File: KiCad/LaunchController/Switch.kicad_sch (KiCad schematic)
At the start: 33 parts, among them SW1 SW_Push, SW11 SW_Push, SW12 SW_Push, SW13 SW_Push, SW14 SW_Push, SW15 SW_Push, SW16 SW_Push, SW17 SW_Push, SW18 SW_Push, SW19 SW_Push, SW2 SW_Push, SW20 SW_Push, SW21 SW_Push, SW22 SW_Push, SW23 SW_Push, SW24 SW_Push, SW25 SW_Push

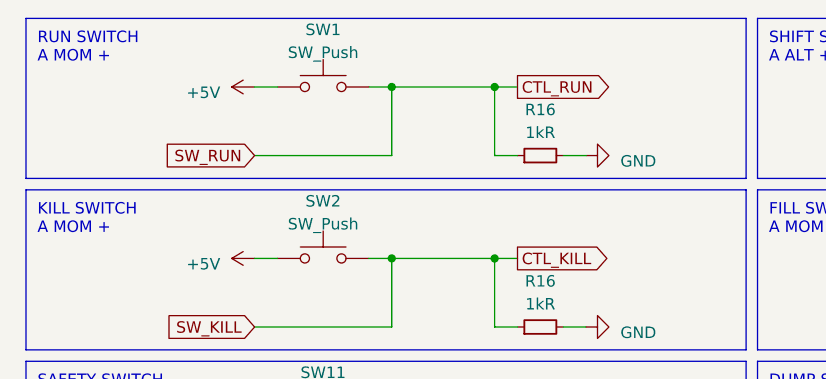
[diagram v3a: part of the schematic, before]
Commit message: RUNスイッチをGND接続に変更
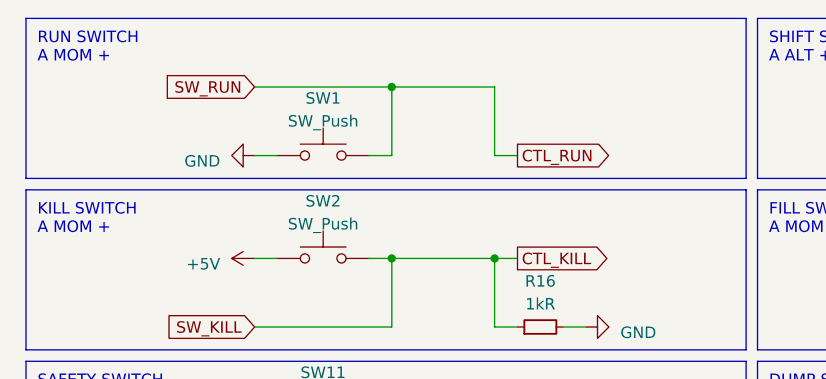
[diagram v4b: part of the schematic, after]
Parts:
- removed R16: 1kR, Resistor_SMD:R_0603_1608Metric_Pad0.98x0.95mm_HandSolder, symbol Device:R_Small
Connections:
- net +5V: no longer SW1.1
- net GND: now also SW1.1
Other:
- moved on the sheet: SW1
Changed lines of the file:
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@@
 (kicad_sch (version 20230121) (generator eeschema)
   (paper "A4")
-  (junction (at 64.77 20.32) (diameter 0) (color 0 0 0 0)
-  )
   (junction (at 146.05 58.42) (diameter 0) (color 0 0 0 0)
   )
@@
   (junction (at 146.05 39.37) (diameter 0) (color 0 0 0 0)
   )
+  (junction (at 134.62 39.37) (diameter 0) (color 0 0 0 0)
+  )
+  (junction (at 146.05 153.67) (diameter 0) (color 0 0 0 0)
+  )
   (junction (at 53.34 20.32) (diameter 0) (color 0 0 0 0)
   )
-  (junction (at 134.62 39.37) (diameter 0) (color 0 0 0 0)
-  )
-  (junction (at 146.05 153.67) (diameter 0) (color 0 0 0 0)
-  )
   (junction (at 53.34 96.52) (diameter 0) (color 0 0 0 0)
   )
@@
     (stroke (width 0) (type default))
   )
-  (wire (pts (xy 38.1 27.94) (xy 53.34 27.94))
-    (stroke (width 0) (type default))
-  )
   (wire (pts (xy 134.62 85.09) (xy 134.62 77.47))
     (stroke (width 0) (type default))
@@
     (stroke (width 0) (type default))
   )
-  (wire (pts (xy 72.39 27.94) (xy 74.93 27.94))
-    (stroke (width 0) (type default))
-  )
   (wire (pts (xy 132.08 77.47) (xy 134.62 77.47))
     (stroke (width 0) (type default))
@@
     (stroke (width 0) (type default))
   )
-  (wire (pts (xy 40.64 20.32) (xy 38.1 20.32))
-    (stroke (width 0) (type default))
-  )
   (wire (pts (xy 53.34 123.19) (xy 53.34 115.57))
     (stroke (width 0) (type default))
@@
     (stroke (width 0) (type default))
   )
-  (wire (pts (xy 64.77 20.32) (xy 67.31 20.32))
-    (stroke (width 0) (type default))
-  )
   (wire (pts (xy 121.92 96.52) (xy 119.38 96.52))
     (stroke (width 0) (type default))
@@
     (stroke (width 0) (type default))
   )
+  (wire (pts (xy 38.1 20.32) (xy 53.34 20.32))
+    (stroke (width 0) (type default))
+  )
   (wire (pts (xy 132.08 134.62) (xy 134.62 134.62))
     (stroke (width 0) (type default))
@@
     (stroke (width 0) (type default))
   )
+  (wire (pts (xy 38.1 27.94) (xy 40.64 27.94))
+    (stroke (width 0) (type default))
+  )
   (wire (pts (xy 134.62 77.47) (xy 146.05 77.47))
     (stroke (width 0) (type default))
@@
     (stroke (width 0) (type default))
   )
-  (wire (pts (xy 50.8 20.32) (xy 53.34 20.32))
+  (wire (pts (xy 50.8 27.94) (xy 53.34 27.94))
     (stroke (width 0) (type default))
   )
@@
     )
   )
-  (global_label "SW_RUN" (shape input) (at 38.1 27.94 180) (fields_autoplaced)
+  (global_label "SW_RUN" (shape input) (at 38.1 20.32 180) (fields_autoplaced)
     (effects (font (size 1.27 1.27)) (justify right))
-    (property "Intersheetrefs" "${INTERSHEET_REFS}" (at 27.6347 27.94 0)
+    (property "Intersheetrefs" "${INTERSHEET_REFS}" (at 27.6347 20.32 0)
       (effects (font (size 1.27 1.27)) (justify right) hide)
     )
@@
     )
   )
-  (global_label "CTL_RUN" (shape output) (at 67.31 20.32 0) (fields_autoplaced)
+  (global_label "CTL_RUN" (shape output) (at 67.31 27.94 0) (fields_autoplaced)
     (effects (font (size 1.27 1.27)) (justify left))
-    (property "Intersheetrefs" "${INTERSHEET_REFS}" (at 78.3801 20.32 0)
+    (property "Intersheetrefs" "${INTERSHEET_REFS}" (at 78.3801 27.94 0)
       (effects (font (size 1.27 1.27)) (justify left) hide)
     )
@@
     )
   )
-  (symbol (lib_id "Device:R_Small") (at 69.85 27.94 90) (unit 1)
-    (in_bom yes) (on_board yes) (dnp no)
-    (property "Reference" "R16" (at 69.85 22.86 90)
-      (effects (font (size 1.27 1.27)))
-    )
-    (property "Value" "1kR" (at 69.85 25.4 90)
-      (effects (font (size 1.27 1.27)))
-    )
-    (property "Footprint" "Resistor_SMD:R_0603_1608Metric_Pad0.98x0.95mm_HandSolder" (at 69.85 27.94 0)
-      (effects (font (size 1.27 1.27)) hide)
-    )
-    (property "Datasheet" "https://www.chip1stop.com/view/dispDetail/DispDetail?partId=ROHM-0021097" (at 69.85 27.94 0)
-      (effects (font (size 1.27 1.27)) hide)
-    )
-    (property "LCSC" "" (at 69.85 27.94 0)
-      (effects (font (size 1.27 1.27)) hide)
-    )
-    (pin "1")
-    (pin "2")
-    (instances
-      (project "LaunchController"
-        (path "/628d040b-43bf-4733-804f-091644a90124"
-          (reference "R16") (unit 1)
-        )
-        (path "/628d040b-43bf-4733-804f-091644a90124/50cfa140-fcaf-4528-b6e7-da7a529677fd"
-          (reference "R49") (unit 1)
-        )
-      )
-      (project "Switch"
-        (path "/7a9db562-9ba2-4e28-86d0-8020190b3bce"
-          (reference "R16") (unit 1)
-        )
-      )
-    )
-  )
-  (symbol (lib_id "power:GND") (at 74.93 27.94 90) (unit 1)
-    (in_bom yes) (on_board yes) (dnp no) (fields_autoplaced)
-    (property "Reference" "#PWR074" (at 81.28 27.94 0)
-      (effects (font (size 1.27 1.27)) hide)
-    )
-    (property "Value" "GND" (at 78.74 28.575 90)
-      (effects (font (size 1.27 1.27)) (justify right))
-    )
-    (property "Footprint" "" (at 74.93 27.94 0)
-      (effects (font (size 1.27 1.27)) hide)
-    )
-    (property "Datasheet" "" (at 74.93 27.94 0)
-      (effects (font (size 1.27 1.27)) hide)
-    )
-    (pin "1")
-    (instances
-      (project "LaunchController"
-        (path "/628d040b-43bf-4733-804f-091644a90124/50cfa140-fcaf-4528-b6e7-da7a529677fd"
-          (reference "#PWR074") (unit 1)
-        )
-      )
-    )
-  )
   (symbol (lib_id "power:+5V") (at 38.1 77.47 90) (unit 1)
     (in_bom yes) (on_board yes) (dnp no) (fields_autoplaced)
@@
         (path "/628d040b-43bf-4733-804f-091644a90124/50cfa140-fcaf-4528-b6e7-da7a529677fd"
           (reference "#PWR0107") (unit 1)
+        )
+      )
+    )
+  )
+  (symbol (lib_id "power:GND") (at 38.1 27.94 270) (unit 1)
+    (in_bom yes) (on_board yes) (dnp no) (fields_autoplaced)
+    (property "Reference" "#PWR06" (at 31.75 27.94 0)
+      (effects (font (size 1.27 1.27)) hide)
+    )
+    (property "Value" "GND" (at 34.29 28.575 90)
+      (effects (font (size 1.27 1.27)) (justify right))
+    )
+    (property "Footprint" "" (at 38.1 27.94 0)
+      (effects (font (size 1.27 1.27)) hide)
+    )
+    (property "Datasheet" "" (at 38.1 27.94 0)
+      (effects (font (size 1.27 1.27)) hide)
+    )
+    (pin "1")
+    (instances
+      (project "LaunchController"
+        (path "/628d040b-43bf-4733-804f-091644a90124/50cfa140-fcaf-4528-b6e7-da7a529677fd"
+          (reference "#PWR06") (unit 1)
         )
       )
@@
     )
   )
-  (symbol (lib_id "Switch:SW_Push") (at 45.72 20.32 0) (unit 1)
-    (in_bom yes) (on_board yes) (dnp no) (fields_autoplaced)
-    (property "Reference" "SW1" (at 45.72 13.97 0)
-      (effects (font (size 1.27 1.27)))
-    )
-    (property "Value" "SW_Push" (at 45.72 16.51 0)
-      (effects (font (size 1.27 1.27)))
-    )
-    (property "Footprint" "TSRP_Button_Switch_SMD:TVAF06-A020B-R" (at 45.72 15.24 0)
-      (effects (font (size 1.27 1.27)) hide)
-    )
-    (property "Datasheet" "https://akizukidenshi.com/catalog/g/gP-14888/" (at 45.72 15.24 0)
+  (symbol (lib_id "Switch:SW_Push") (at 45.72 27.94 0) (unit 1)
+    (in_bom yes) (on_board yes) (dnp no) (fields_autoplaced)
+    (property "Reference" "SW1" (at 45.72 21.59 0)
+      (effects (font (size 1.27 1.27)))
+    )
+    (property "Value" "SW_Push" (at 45.72 24.13 0)
+      (effects (font (size 1.27 1.27)))
+    )
+    (property "Footprint" "TSRP_Button_Switch_SMD:TVAF06-A020B-R" (at 45.72 22.86 0)
+      (effects (font (size 1.27 1.27)) hide)
+    )
+    (property "Datasheet" "https://akizukidenshi.com/catalog/g/gP-14888/" (at 45.72 22.86 0)
       (effects (font (size 1.27 1.27)) hide)
     )
@@
         )
       )
-    )
-  )
-  (symbol (lib_id "power:+5V") (at 38.1 20.32 90) (unit 1)
-    (in_bom yes) (on_board yes) (dnp no) (fields_autoplaced)
-    (property "Reference" "#PWR073" (at 41.91 20.32 0)
-      (effects (font (size 1.27 1.27)) hide)
-    )
-    (property "Value" "+5V" (at 34.29 20.955 90)
-      (effects (font (size 1.27 1.27)) (justify left))
-    )
-    (property "Footprint" "" (at 38.1 20.32 0)
-      (effects (font (size 1.27 1.27)) hide)
-    )
-    (property "Datasheet" "" (at 38.1 20.32 0)
-      (effects (font (size 1.27 1.27)) hide)
-    )
-    (pin "1")
-    (instances
-      (project "LaunchController"
-        (path "/628d040b-43bf-4733-804f-091644a90124/50cfa140-fcaf-4528-b6e7-da7a529677fd"
-          (reference "#PWR073") (unit 1)
-        )
-      )

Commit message: KiCad9.0に対応
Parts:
- renumbered R16 to R50, R16 to R51, R16 to R52, R16 to R54, R16 to R55, R16 to R56, R16 to R57, R16 to R59, R16 to R60, R16 to R61, R16 to R62, R16 to R63, R16 to R64, R16 to R65, R16 to R66
